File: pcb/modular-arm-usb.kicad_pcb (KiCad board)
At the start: 2 copper layers, 24 parts, among them CON1 ARM-SWD-HEADER, IC1 LPC11U14FBD48, P1 USB, P2 UNFUSED_PWR, P3 BATT, P4 GPIO, P5 BATT, U2 LD1117V33, U3 NRF24L01+

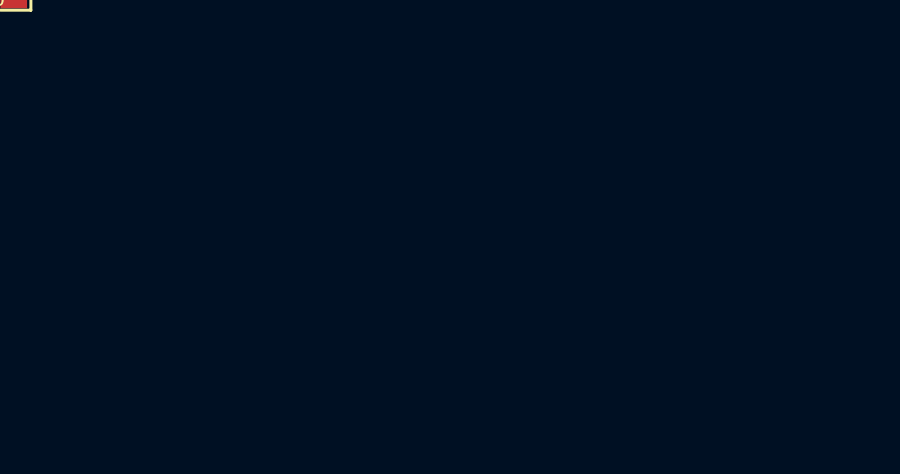
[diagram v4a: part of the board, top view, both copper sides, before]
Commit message: added LED, and removed VLED from power sheet
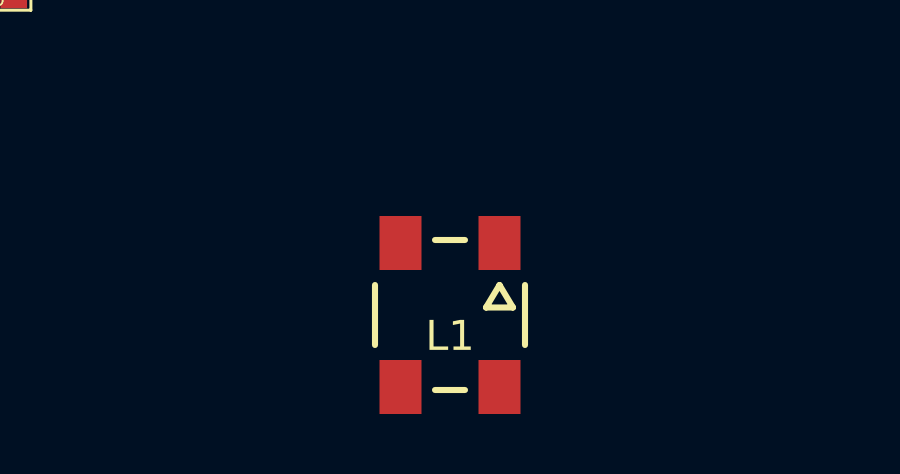
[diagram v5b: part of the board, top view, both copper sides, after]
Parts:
- added L1: PP_WS2812B, WS2812B_PP, F.Cu at (190.2, 127.5)
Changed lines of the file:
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@@
 (kicad_pcb (version 3) (host pcbnew "(2013-07-07 BZR 4022)-stable")
   (general
-    (links 49)
-    (no_connects 49)
+    (links 51)
+    (no_connects 51)
     (area 0 0 0 0)
     (thickness 1.6)
@@
     (tracks 0)
     (zones 0)
-    (modules 24)
+    (modules 25)
     (nets 17)
   )
@@
   (net 9 LPC_USB_DM)
   (net 10 LPC_USB_DP)
-  (net 11 N-0000019)
-  (net 12 N-0000021)
-  (net 13 N-0000022)
-  (net 14 N-0000065)
-  (net 15 N-0000066)
+  (net 11 N-0000021)
+  (net 12 N-0000022)
+  (net 13 N-0000023)
+  (net 14 N-0000067)
+  (net 15 N-0000068)
   (net 16 VUSB)
   (net_class Default "This is the default net class."
@@
     (add_net LPC_USB_DM)
     (add_net LPC_USB_DP)
-    (add_net N-0000019)
     (add_net N-0000021)
     (add_net N-0000022)
-    (add_net N-0000065)
-    (add_net N-0000066)
+    (add_net N-0000023)
+    (add_net N-0000067)
+    (add_net N-0000068)
     (add_net VUSB)
   )
@@
     (pad 1 smd rect (at -2.54 1.95) (size 0.76 2.4)
       (layers F.Cu F.Paste F.Mask)
-      (net 11 N-0000019)
+      (net 11 N-0000021)
     )
     (pad 2 smd rect (at -2.54 -1.95) (size 0.76 2.4)
@@
     (pad 7 smd rect (at -4.5 0.25) (size 2 0.25)
       (layers F.Cu F.Paste F.Mask)
-      (net 12 N-0000021)
+      (net 12 N-0000022)
     )
     (pad 6 smd rect (at -4.5 -0.25) (size 2 0.25)
       (layers F.Cu F.Paste F.Mask)
-      (net 13 N-0000022)
+      (net 13 N-0000023)
     )
     (pad 5 smd rect (at -4.5 -0.75) (size 2 0.25)
@@
     (pad 1 smd rect (at -1.651 0) (size 1.524 2.032)
       (layers F.Cu F.Paste F.Mask)
-      (net 15 N-0000066)
+      (net 15 N-0000068)
     )
     (pad 2 smd rect (at 1.651 0) (size 1.524 2.032)
@@
     (pad 1 smd rect (at -0.9525 0) (size 0.889 1.397)
       (layers F.Cu F.Paste F.Mask)
-      (net 15 N-0000066)
+      (net 15 N-0000068)
     )
     (pad 2 smd rect (at 0.9525 0) (size 0.889 1.397)
@@
     (pad 2 smd rect (at 0.9525 0) (size 0.889 1.397)
       (layers F.Cu F.Paste F.Mask)
-      (net 12 N-0000021)
+      (net 12 N-0000022)
     )
     (model smd/chip_cms.wrl
@@
     (pad 2 smd rect (at 0.9525 0) (size 0.889 1.397)
       (layers F.Cu F.Paste F.Mask)
-      (net 13 N-0000022)
+      (net 13 N-0000023)
     )
     (model smd/chip_cms.wrl
@@
     (pad 2 smd rect (at 0.9525 0) (size 0.889 1.397)
       (layers F.Cu F.Paste F.Mask)
-      (net 11 N-0000019)
+      (net 11 N-0000021)
     )
     (model smd/chip_cms.wrl
@@
     (pad 2 smd rect (at 1 0) (size 1 4.5)
       (layers F.Cu F.Paste F.Mask)
-      (net 14 N-0000065)
+      (net 14 N-0000067)
     )
     (pad NC smd rect (at -3.35 -5.1) (size 1.5 3.4)
@@
     (pad 1 thru_hole rect (at -1.27 0) (size 1.524 1.524) (drill 1.016)
       (layers *.Cu *.Mask F.SilkS)
-      (net 15 N-0000066)
+      (net 15 N-0000068)
     )
     (pad 2 thru_hole circle (at 1.27 0) (size 1.524 1.524) (drill 1.016)
@@
     (pad 3 thru_hole circle (at 5.08 0) (size 1.778 1.778) (drill 1.125)
       (layers *.Cu *.Mask F.SilkS)
-      (net 15 N-0000066)
+      (net 15 N-0000068)
     )
   )
@@
     (pad 1 thru_hole rect (at -1.27 0) (size 1.524 1.524) (drill 1.016)
       (layers *.Cu *.Mask F.SilkS)
-      (net 14 N-0000065)
+      (net 14 N-0000067)
     )
     (pad 2 thru_hole circle (at 1.27 0) (size 1.524 1.524) (drill 1.016)
@@
     )
   )
+  (module WS2812B_PP (layer F.Cu)
+    (at 190.246 127.508)
+    (fp_text reference L1 (at 0 0.7) (layer F.SilkS)
+      (effects (font (size 1 1) (thickness 0.2)))
+    )
+    (fp_text value PP_WS2812B (at 0 4.85) (layer F.SilkS) hide
+      (effects (font (size 1 1) (thickness 0.2)))
+    )
+    (fp_line (start 1.65 -1) (end 1.2 -0.25) (layer F.SilkS) (width 0.2032))
+    (fp_line (start 1.2 -0.25) (end 2.1 -0.25) (layer F.SilkS) (width 0.2032))
+    (fp_line (start 2.1 -0.25) (end 1.65 -1) (layer F.SilkS) (width 0.2032))
+    (fp_line (start -2.5 -1) (end -2.5 1) (layer F.SilkS) (width 0.2032))
+    (fp_line (start -0.5 2.5) (end 0.5 2.5) (layer F.SilkS) (width 0.2032))
+    (fp_line (start 2.5 -1) (end 2.5 1) (layer F.SilkS) (width 0.2032))
+    (fp_line (start -0.5 -2.5) (end 0.5 -2.5) (layer F.SilkS) (width 0.2032))
+    (fp_line (start 2.1 2.5) (end 2.5 2.5) (layer Dwgs.User) (width 0.2032))
+    (fp_line (start -1.2 2.5) (end 1.2 2.5) (layer Dwgs.User) (width 0.2032))
+    (fp_line (start -2.5 2.5) (end -2.1 2.5) (layer Dwgs.User) (width 0.2032))
+    (fp_line (start 2.1 -2.5) (end 2.5 -2.5) (layer Dwgs.User) (width 0.2032))
+    (fp_line (start -1.2 -2.5) (end 1.2 -2.5) (layer Dwgs.User) (width 0.2032))
+    (fp_line (start -2.5 -2.5) (end -2.1 -2.5) (layer Dwgs.User) (width 0.2032))
+    (fp_line (start -2.1 -2.7) (end -1.2 -2.7) (layer Dwgs.User) (width 0.2032))
+    (fp_line (start -1.2 -2.7) (end -1.2 -1.8) (layer Dwgs.User) (width 0.2032))
+    (fp_line (start -1.2 -1.8) (end -2.1 -1.8) (layer Dwgs.User) (width 0.2032))
+    (fp_line (start -2.1 -1.8) (end -2.1 -2.7) (layer Dwgs.User) (width 0.2032))
+    (fp_line (start 2.1 -2.7) (end 1.2 -2.7) (layer Dwgs.User) (width 0.2032))
+    (fp_line (start 1.2 -2.7) (end 1.2 -1.8) (layer Dwgs.User) (width 0.2032))
+    (fp_line (start 1.2 -1.8) (end 2.1 -1.8) (layer Dwgs.User) (width 0.2032))
+    (fp_line (start 2.1 -1.8) (end 2.1 -2.7) (layer Dwgs.User) (width 0.2032))
+    (fp_line (start -2.1 2.7) (end -2.1 1.8) (layer Dwgs.User) (width 0.2))
+    (fp_line (start -2.1 1.8) (end -1.2 1.8) (layer Dwgs.User) (width 0.2))
+    (fp_line (start -1.2 1.8) (end -1.2 2.7) (layer Dwgs.User) (width 0.2))
+    (fp_line (start -1.2 2.7) (end -2.1 2.7) (layer Dwgs.User) (width 0.2))
+    (fp_line (start 1.2 2.7) (end 1.2 1.8) (layer Dwgs.User) (width 0.2))
+    (fp_line (start 1.2 1.8) (end 2.1 1.8) (layer Dwgs.User) (width 0.2))
+    (fp_line (start 2.1 1.8) (end 2.1 2.7) (layer Dwgs.User) (width 0.2))
+    (fp_line (start 2.1 2.7) (end 1.2 2.7) (layer Dwgs.User) (width 0.2))
+    (fp_line (start 2.5 -2.5) (end 2.5 2.5) (layer Dwgs.User) (width 0.2))
+    (fp_line (start -2.49936 2.49936) (end -2.49936 -2.49936) (layer Dwgs.User) (width 0.2))
+    (pad 3 smd rect (at 1.65 -2.4) (size 1.4 1.8)
+      (layers F.Cu F.Paste F.Mask)
+      (net 8 GND)
+    )
+    (pad 4 smd rect (at -1.65 -2.4) (size 1.4 1.8)
+      (layers F.Cu F.Paste F.Mask)
+    )
+    (pad 1 smd rect (at -1.65 2.4) (size 1.4 1.8)
+      (layers F.Cu F.Paste F.Mask)
+      (net 7 3V3)
+    )
+    (pad 2 smd rect (at 1.65 2.4) (size 1.4 1.8)
+      (layers F.Cu F.Paste F.Mask)
+    )
+  )

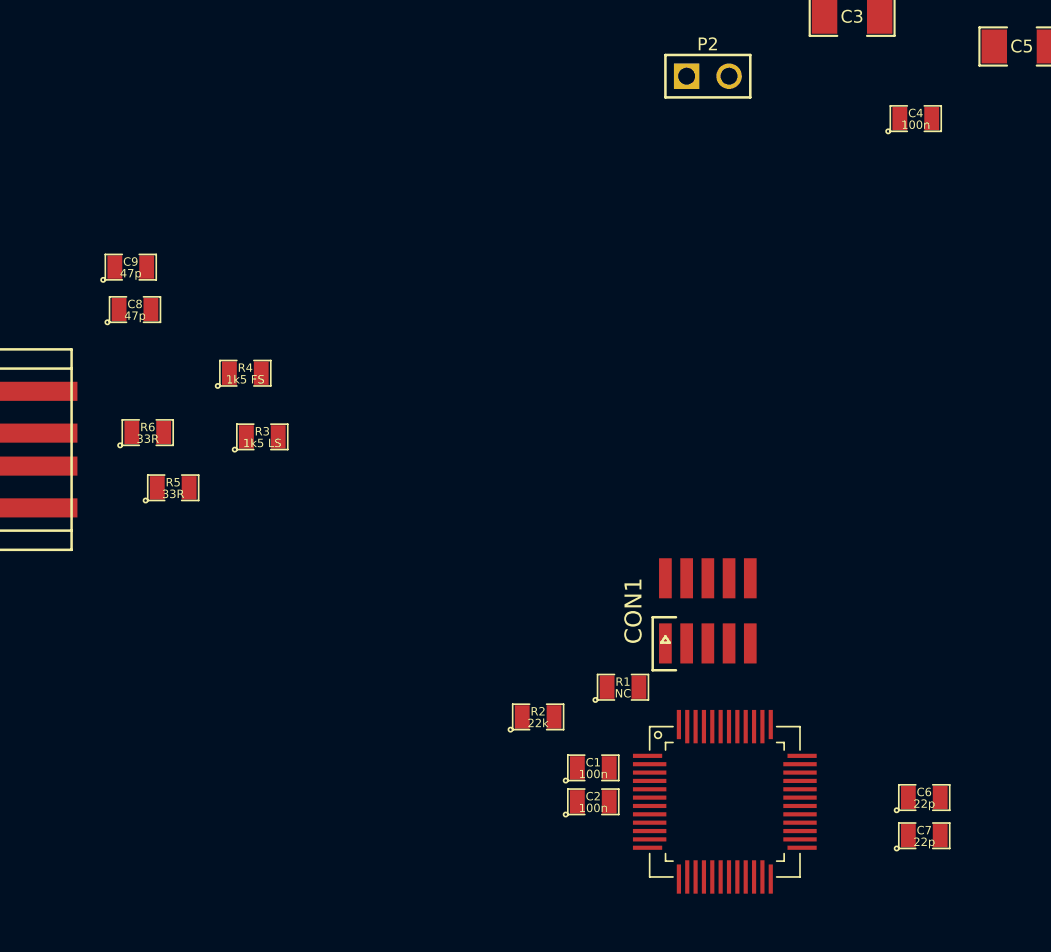
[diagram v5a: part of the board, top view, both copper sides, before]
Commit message: some labels, and changed sm0805 parts to use my nosilkscreen package
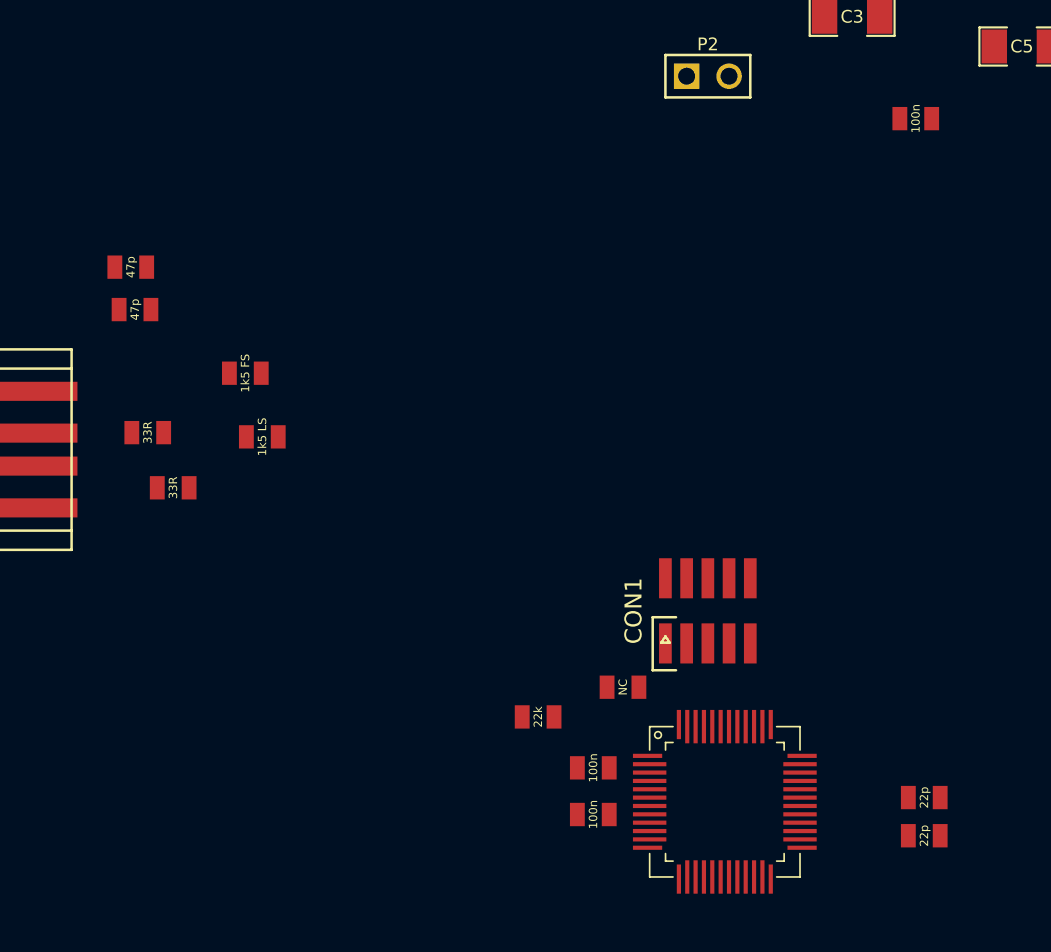
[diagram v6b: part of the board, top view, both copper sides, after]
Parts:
- C1, C2, C4, C6, C7, C8, C9, R1, R2, R3, R4, R5, R6: footprint SM0805 -> SM0805_NOSILKSCREEN
- moved C2 0.76 mm to (154.9, 115.3)
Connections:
- net N-0000022 renamed /lpc-mcu/XTALOUT
- net N-0000023 renamed /lpc-mcu/XTALIN
- IC1 pad 25: (no net) -> /lpc-mcu/LED_INPUT
- L1 pad 4: (no net) -> /lpc-mcu/LED_INPUT

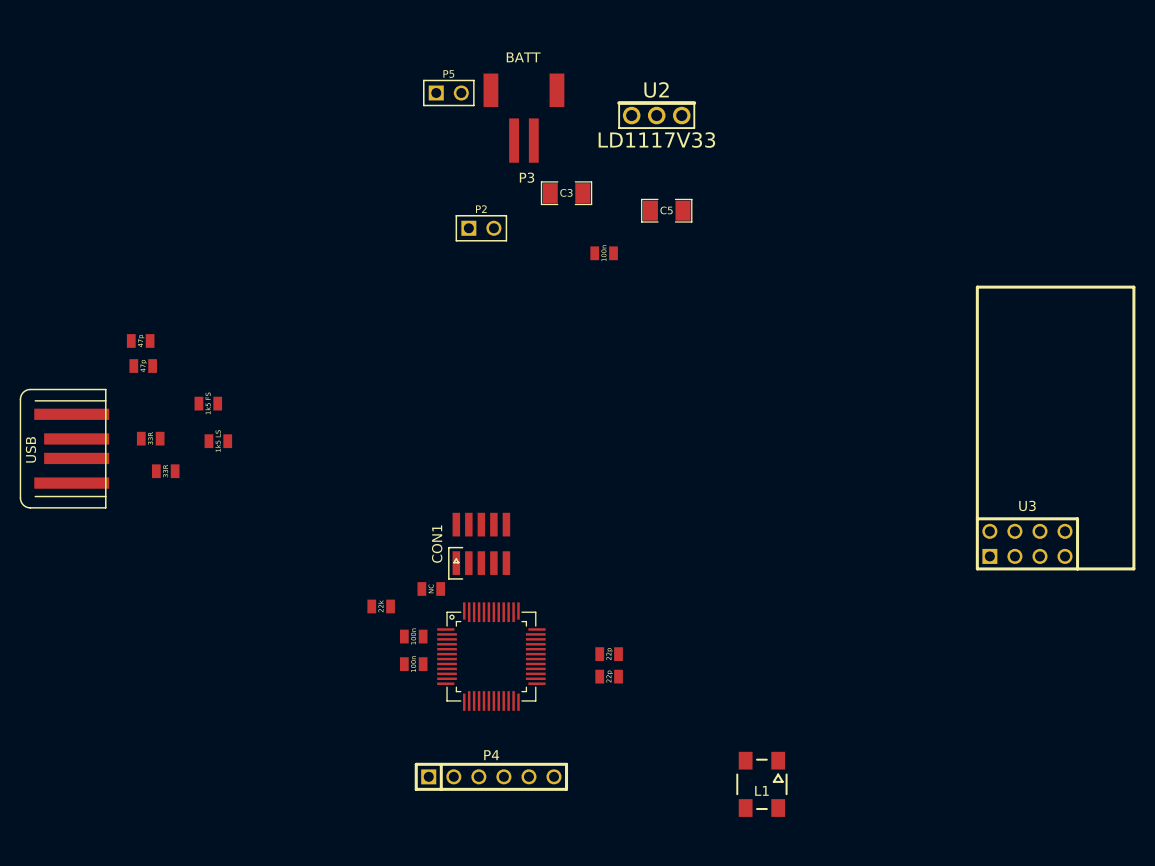
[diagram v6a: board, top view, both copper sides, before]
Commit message: gpios and rf24 connections
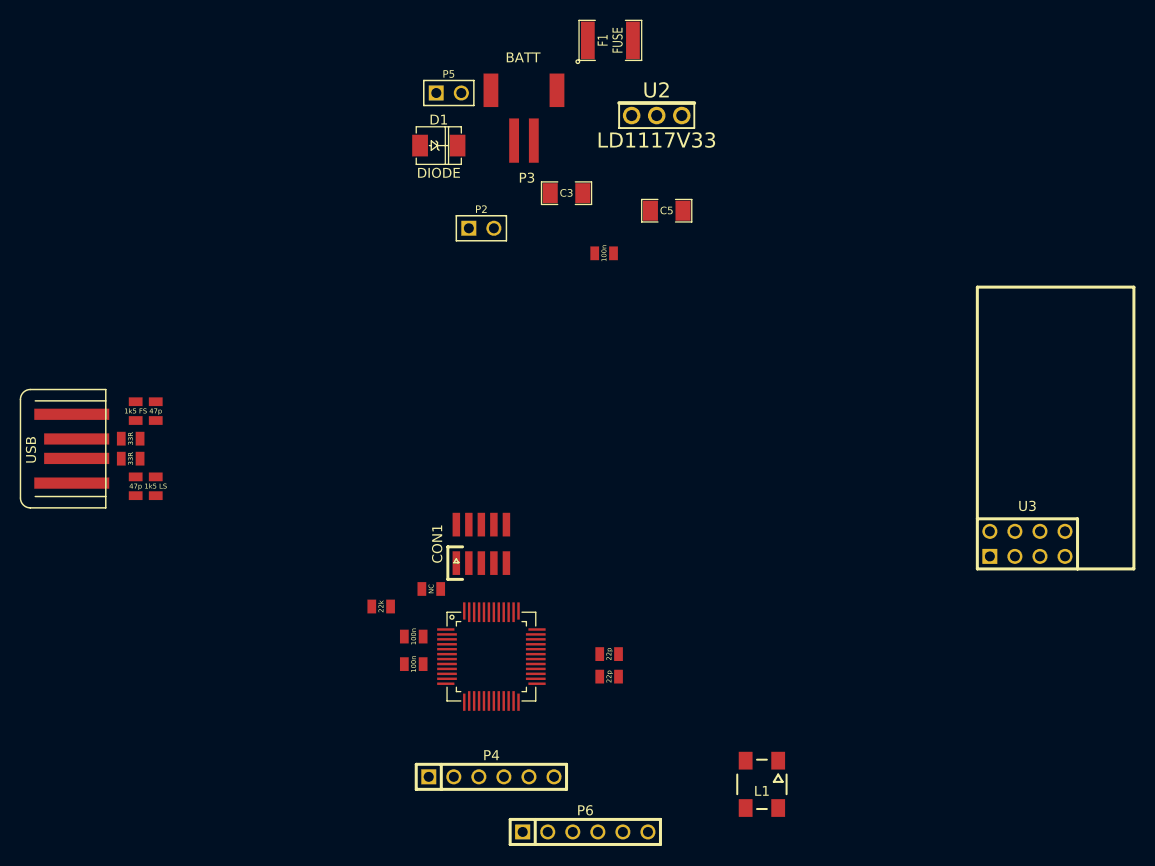
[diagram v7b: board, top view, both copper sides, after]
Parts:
- added D1: DIODE, DO-214AC(SMA), F.Cu at (157.5, 62.7)
- added F1: FUSE, SM1812, F.Cu at (174.9, 52.1)
- added P6: GPIO2, PIN_ARRAY-6X1, F.Cu at (172.3, 132.3)
- moved C8 12.2 mm to (126.7, 97.3), turned to 270 degrees
- moved R3 7.82 mm to (128.8, 97.3), turned to 90 degrees
- moved R4 7.41 mm to (126.7, 89.7), turned to 270 degrees
- moved C9 7.27 mm to (128.8, 89.7), turned to 90 degrees
- moved R5 3.78 mm to (126.2, 94.5)
- moved R6 2.03 mm to (126.2, 92.5)
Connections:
- IC1 pad 10: (no net) -> RF24_CSN
- IC1 pad 11: (no net) -> /lpc-mcu/RXD
- IC1 pad 12: (no net) -> /lpc-mcu/TXD
- IC1 pad 13: (no net) -> /lpc-mcu/SCK1
- IC1 pad 15: (no net) -> /lpc-mcu/SCL
- IC1 pad 16: (no net) -> /lpc-mcu/SDA
- IC1 pad 17: (no net) -> /lpc-mcu/MOSI1
- IC1 pad 18: (no net) -> /lpc-mcu/SSEL1
- IC1 pad 23: (no net) -> /lpc-mcu/LED_INPUT
- IC1 pad 24: (no net) -> RF24_IRQ
- IC1 pad 25: /lpc-mcu/LED_INPUT -> RF24_CE
- IC1 pad 26: (no net) -> /lpc-mcu/MISO1
- IC1 pad 27: (no net) -> RF24_MISO
- IC1 pad 28: (no net) -> RF24_MOSI
- IC1 pad 31: (no net) -> RF24_SCK
- IC1 pad 32: (no net) -> /lpc-mcu/AD0
- IC1 pad 33: (no net) -> /lpc-mcu/AD1
- P4 pad 1: (no net) -> GND
- P4 pad 2: (no net) -> 3V3
- P4 pad 3: (no net) -> /lpc-mcu/SCL
- P4 pad 4: (no net) -> /lpc-mcu/SDA
- P4 pad 5: (no net) -> /lpc-mcu/RXD
- P4 pad 6: (no net) -> /lpc-mcu/TXD
- U3 pad 3: (no net) -> RF24_CE
- U3 pad 4: (no net) -> RF24_CSN
- U3 pad 5: (no net) -> RF24_SCK
- U3 pad 6: (no net) -> RF24_MOSI
- U3 pad 7: (no net) -> RF24_MISO
- U3 pad 8: (no net) -> RF24_IRQ
